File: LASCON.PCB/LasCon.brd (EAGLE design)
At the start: 44.4 x 28 mm, 11 parts

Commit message: Added LED & 3rd laser
Added LED and 3rd laser, with pingpong ball outline
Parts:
- added U$11: LASER, GW-devices:LASER
- added U$12, U$14, U$15, U$16: 24, GW-devices:RF-C0805
- added U$13: LED5060A, GW-devices:PLCC-6
- moved IC1 33.9 mm to (27.6, 14.8), flipped to the top, turned to 270 degrees
- moved U$5 32.1 mm to (6.90, 19.4), flipped to the top, turned to 180 degrees
- moved U$3 30.8 mm to (-0.35, 18.4), flipped to the top
- moved U$10 28.3 mm to (33.2, -18.6), flipped to the top
- moved U$4 28.0 mm to (6.90, 17.2), flipped to the top
- moved U$7 0.10 mm to (0.00, 3.75)
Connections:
- new net N$11: U$12.2, U$3.6
- new net N$12: U$13.4, U$14.2
- new net N$13: U$13.5, U$15.2
- new net N$14: U$13.6, U$16.2
- new net N$4: U$11.2, U$13.1, U$3.8
- net +3V3: now also U$11.1
- net GND: now also U$12.1
- net N$2: now also U$13.3
- net N$3: now also U$13.2
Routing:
- net N$4: track 0.00 -> 88.2 mm, vias 0 -> 1
- net N$2: track 5.05 -> 69.7 mm, vias 0 -> 1
- net N$1: track 42.9 -> 0.00 mm, vias 1 -> 0
- net N$5: track 38.9 -> 0.00 mm
- net N$3: track 16.0 -> 54.1 mm, vias 0 -> 1
- net N$6: track 29.3 -> 0.00 mm
- net +3V3: track 37.6 -> 20.0 mm
- net N$7: track 42.6 -> 28.1 mm
- net N$10: track 12.9 -> 3.76 mm
- net N$9: track 10.2 -> 4.13 mm
- net N$8: track 39.7 -> 34.3 mm
- net N$11: track 0.00 -> 3.97 mm
- net N$14: track 0.00 -> 3.14 mm
- net N$12: track 0.00 -> 3.03 mm
- net N$13: track 0.00 -> 2.79 mm
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- removed copper zone on layer 1, net GND
- removed copper zone on layer 16, net GND
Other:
- board size 44.4 x 28 mm -> 44.4 x 58 mm

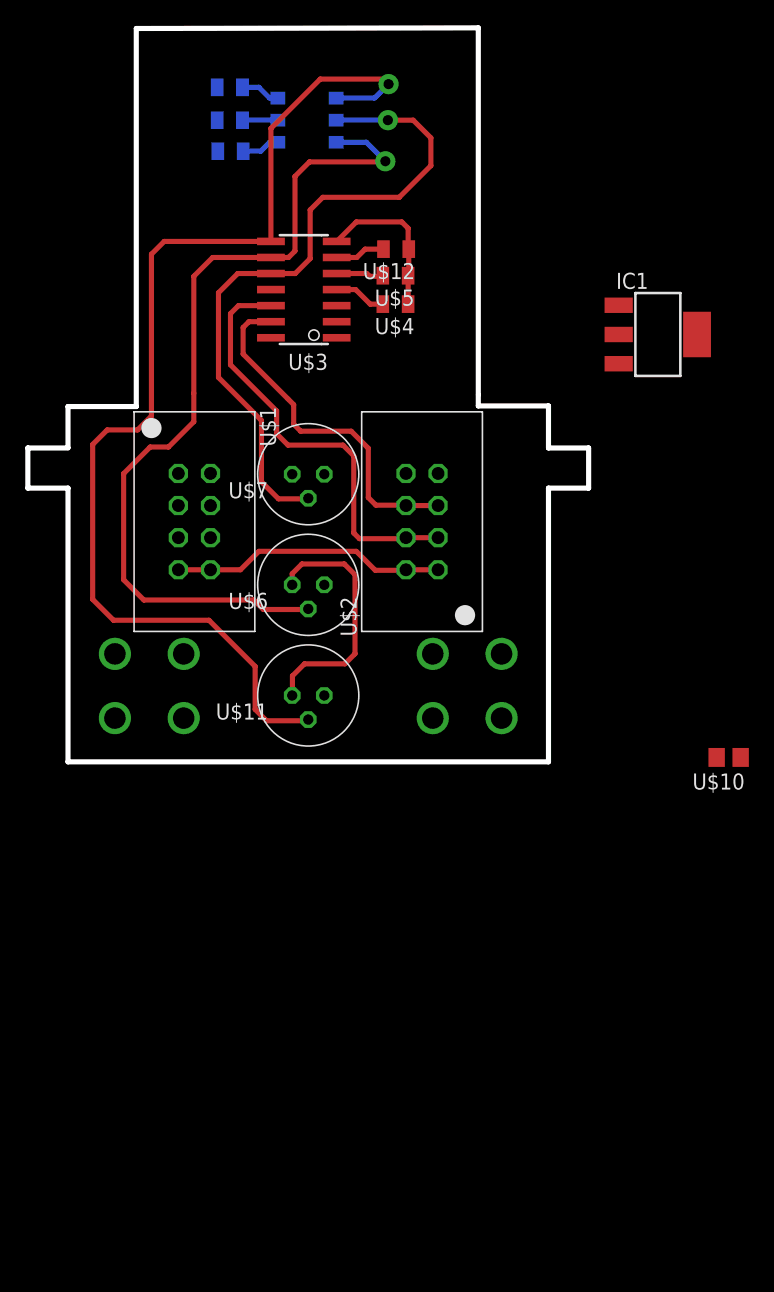
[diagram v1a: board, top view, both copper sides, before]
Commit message: Completed laser board
Finished routing, may need to redo flipped.
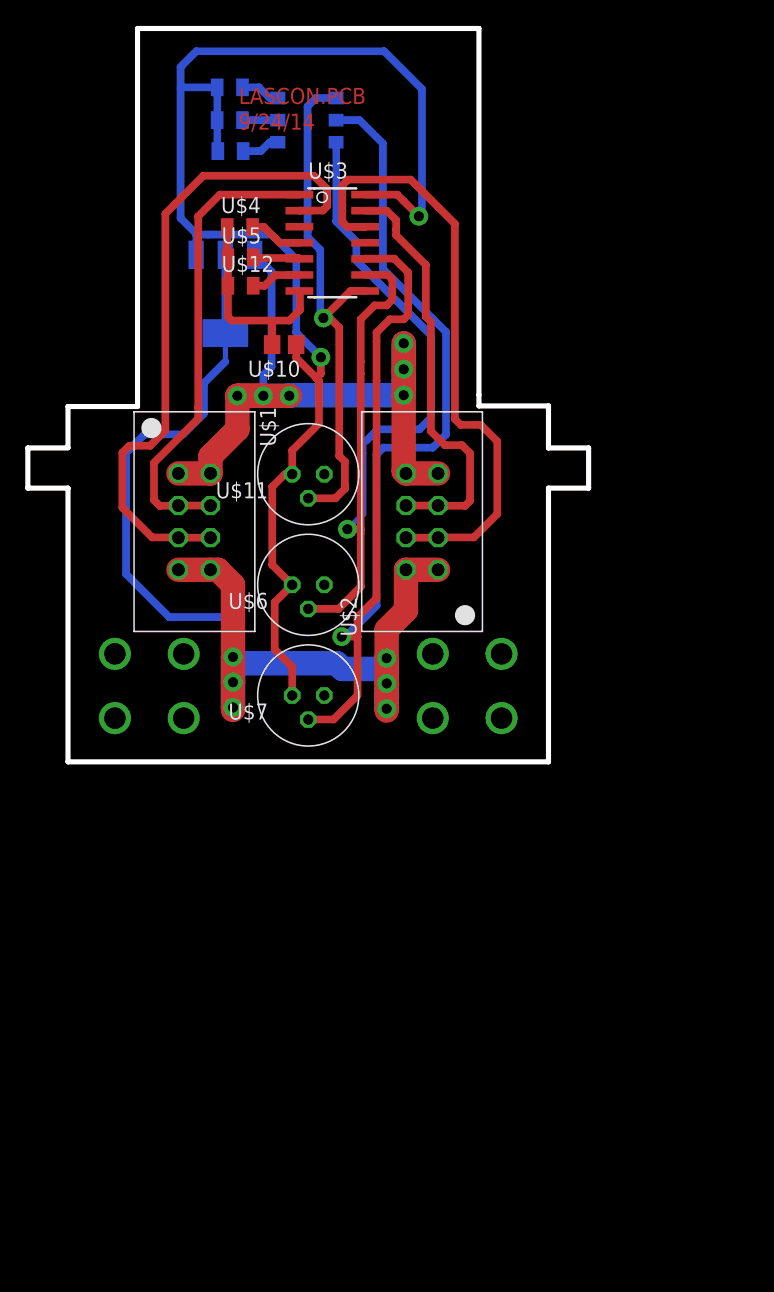
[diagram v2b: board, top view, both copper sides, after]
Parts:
- moved U$10 48.0 mm to (-1.90, 14.0)
- moved IC1 34.3 mm to (-6.55, 18.0), flipped to the bottom, turned to 180 degrees
- moved U$11 17.5 mm to (0.00, 3.75)
- moved U$7 17.5 mm to (0.00, -13.8)
- moved U$4 13.7 mm to (-5.40, 23.3), turned to 0 degrees
- moved U$12 12.6 mm to (-5.35, 18.6), turned to 0 degrees
- moved U$5 12.3 mm to (-5.35, 20.9), turned to 0 degrees
- moved U$3 4.33 mm to (1.90, 22.1), turned to 270 degrees
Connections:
- net +3V3: now also U$14.1, U$15.1, U$16.1
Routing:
- net +3V3: track 20.0 -> 112.2 mm, vias 0 -> 2
- net GND: track 34.4 -> 110.7 mm, vias 0 -> 6
- net N$1: track 0.00 -> 57.9 mm, vias 0 -> 6
- net N$6: track 0.00 -> 51.8 mm
- net N$4: track 88.2 -> 41.8 mm
- net N$3: track 54.1 -> 97.0 mm
- net N$5: track 0.00 -> 37.3 mm
- net N$8: track 34.3 -> 48.7 mm
- net N$7: track 28.1 -> 33.4 mm
- net N$2: track 69.7 -> 72.8 mm
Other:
- outline, holes or cut-outs redrawn
- board text added: "LASCON.PCB 9/24/14"

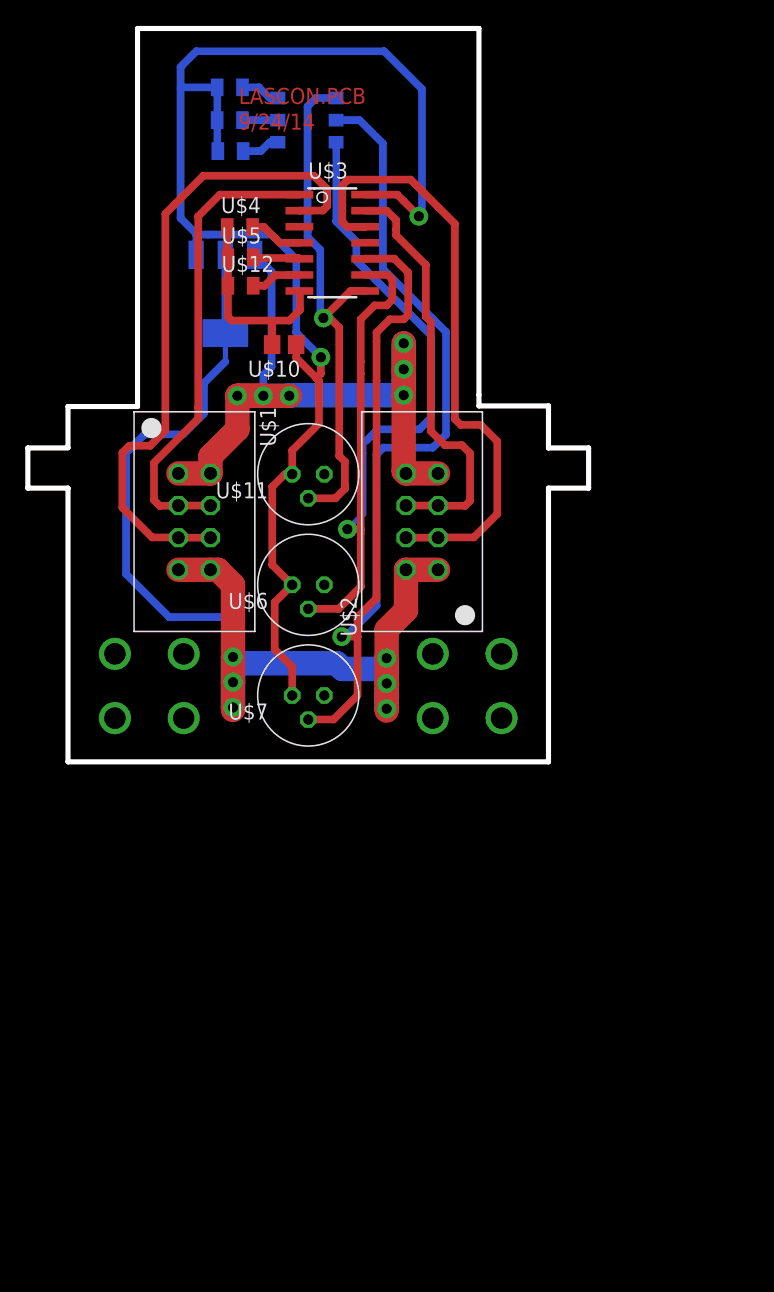
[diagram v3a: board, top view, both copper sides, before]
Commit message: Flipped LasCon
Reversed orientation, small traces though
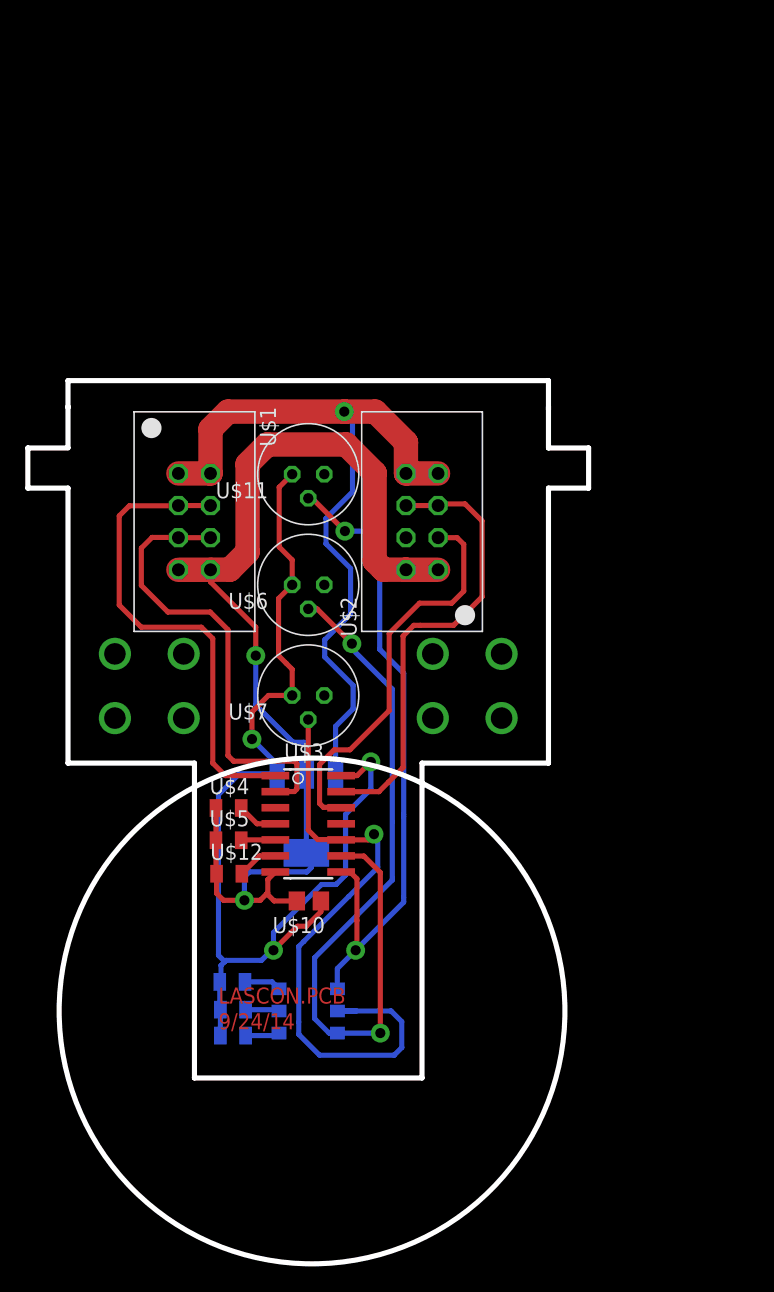
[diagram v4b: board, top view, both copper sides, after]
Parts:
- moved U$16 70.8 mm to (-6.00, -36.4)
- moved U$13 70.5 mm to (0.00, -38.7)
- moved U$15 70.4 mm to (-5.95, -38.6)
- moved U$14 70.0 mm to (-5.95, -40.6)
- moved U$12 46.5 mm to (-6.25, -27.9)
- moved U$5 46.1 mm to (-6.30, -25.2)
- moved U$3 46.0 mm to (0.00, -23.9)
- moved U$4 46.0 mm to (-6.30, -22.6)
- moved U$10 44.0 mm to (0.05, -30.0)
- moved IC1 41.6 mm to (-0.15, -23.1)
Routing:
- net N$3: track 97.0 -> 51.1 mm
- net +3V3: track 112.2 -> 85.1 mm, vias 2 -> 3
- net GND: track 110.7 -> 87.4 mm, vias 6 -> 2
- net N$8: track 48.7 -> 31.5 mm
- net N$6: track 51.8 -> 36.5 mm
- net N$2: track 72.8 -> 60.1 mm, vias 1 -> 2
- net N$4: track 41.8 -> 52.5 mm, vias 1 -> 2
- net N$1: track 57.9 -> 61.1 mm, vias 6 -> 1
- net N$7: track 33.4 -> 36.3 mm
- net N$5: track 37.3 -> 38.3 mm
- net N$9: track 4.22 -> 3.22 mm
- net N$10: track 3.70 -> 2.71 mm
- net N$11: track 4.01 -> 3.23 mm
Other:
- board size 44.4 x 58 mm -> 44.4 x 69.9 mm

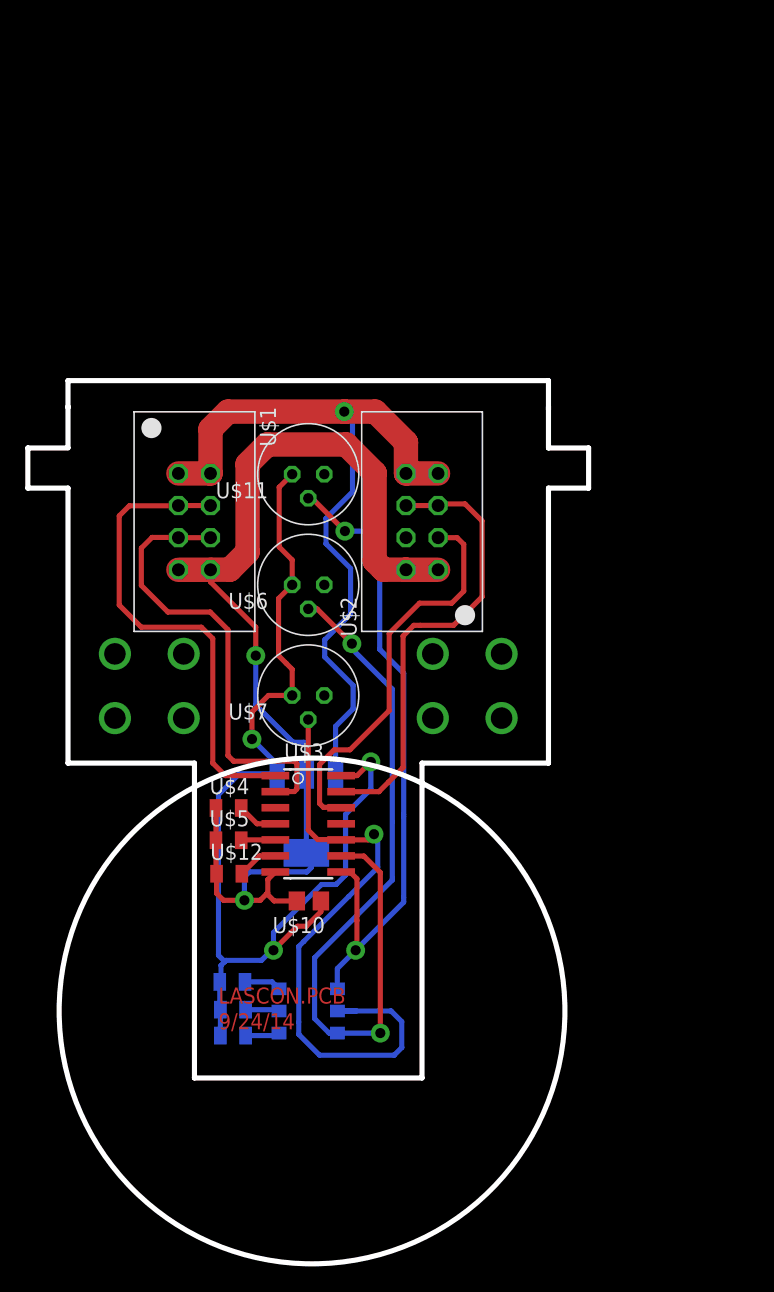
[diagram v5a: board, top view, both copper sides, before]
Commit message: PosCon parts, KW2 frontend, LasCon
Added part numbers for orange display, black buttons to PosCon. Worked
on frontend layout for KW2 and produced a new version of LasCon
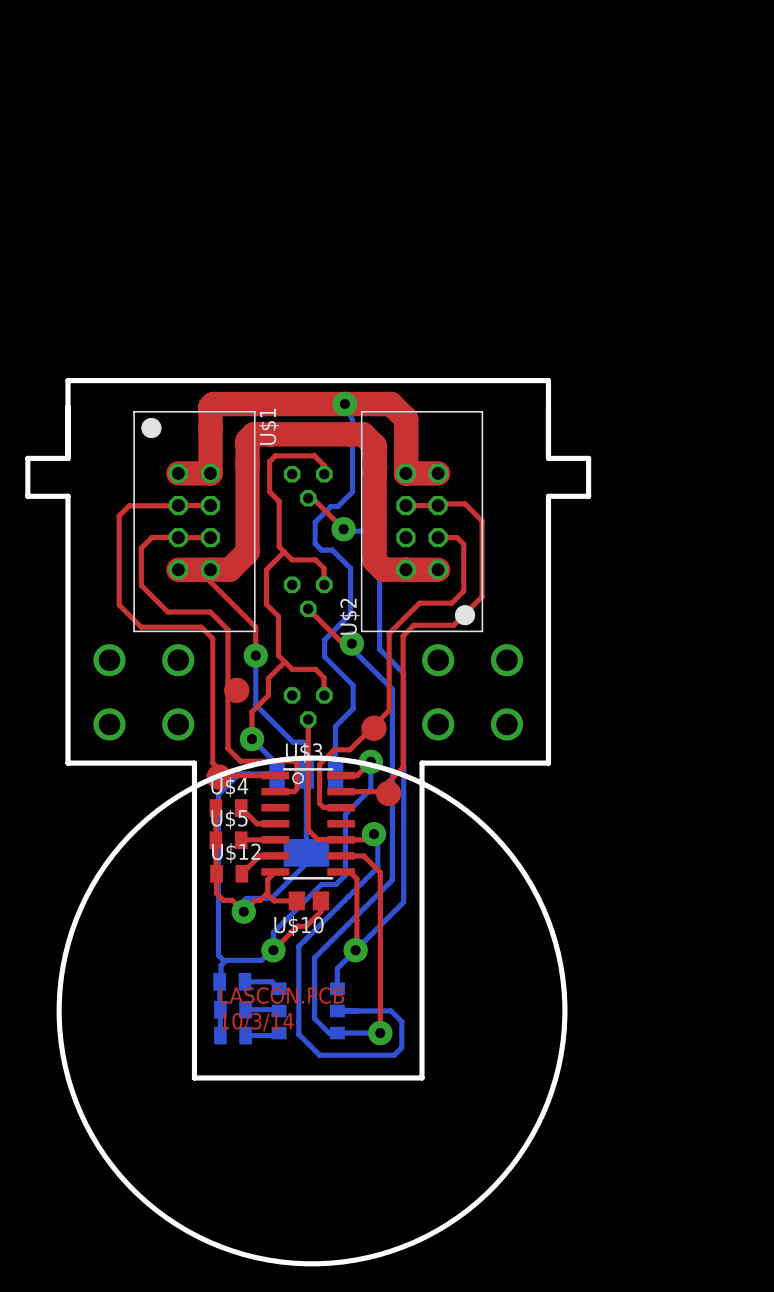
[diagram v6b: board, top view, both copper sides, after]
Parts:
- moved U$8 0.66 mm to (-13.0, -13.5)
- moved U$9 0.66 mm to (13.0, -13.5)
- flipped U$11 to the bottom
- flipped U$6 to the bottom
- flipped U$7 to the bottom
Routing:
- net +3V3: track 85.1 -> 100.2 mm
- net N$1: track 61.1 -> 65.7 mm
- net GND: track 87.4 -> 90.8 mm
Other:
- outline, holes or cut-outs redrawn
- board text added: "LASCON.PCB 10/3/14"
- board text removed: "LASCON.PCB 9/24/14"
